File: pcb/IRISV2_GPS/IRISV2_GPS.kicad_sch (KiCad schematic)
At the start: 22 parts, among them U1 NEO-M9N, U2 lna

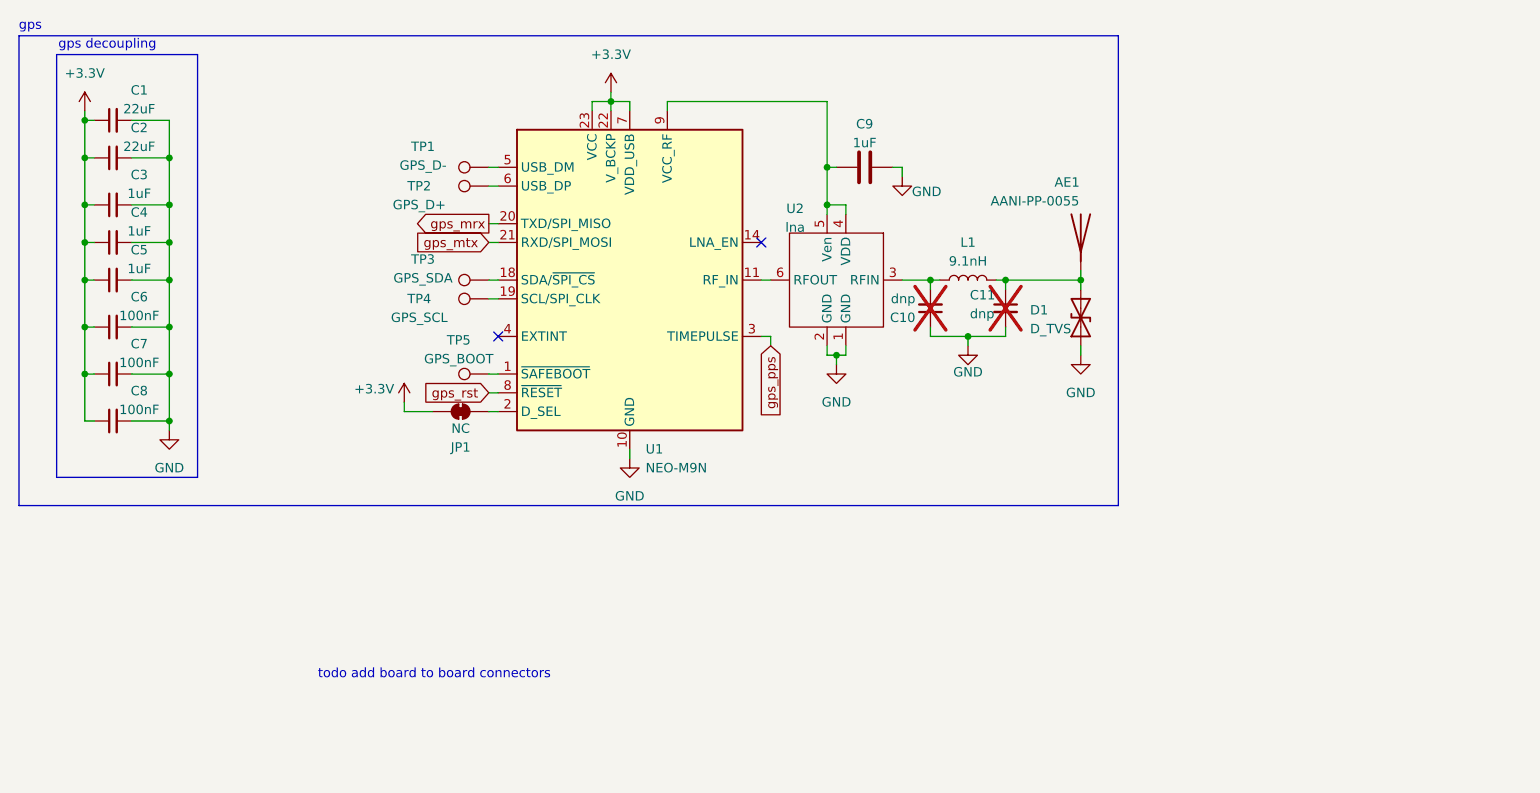
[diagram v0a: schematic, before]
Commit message: gps finished minus tvs (WHY ARE THEY ALL 0201), top layout + routing started
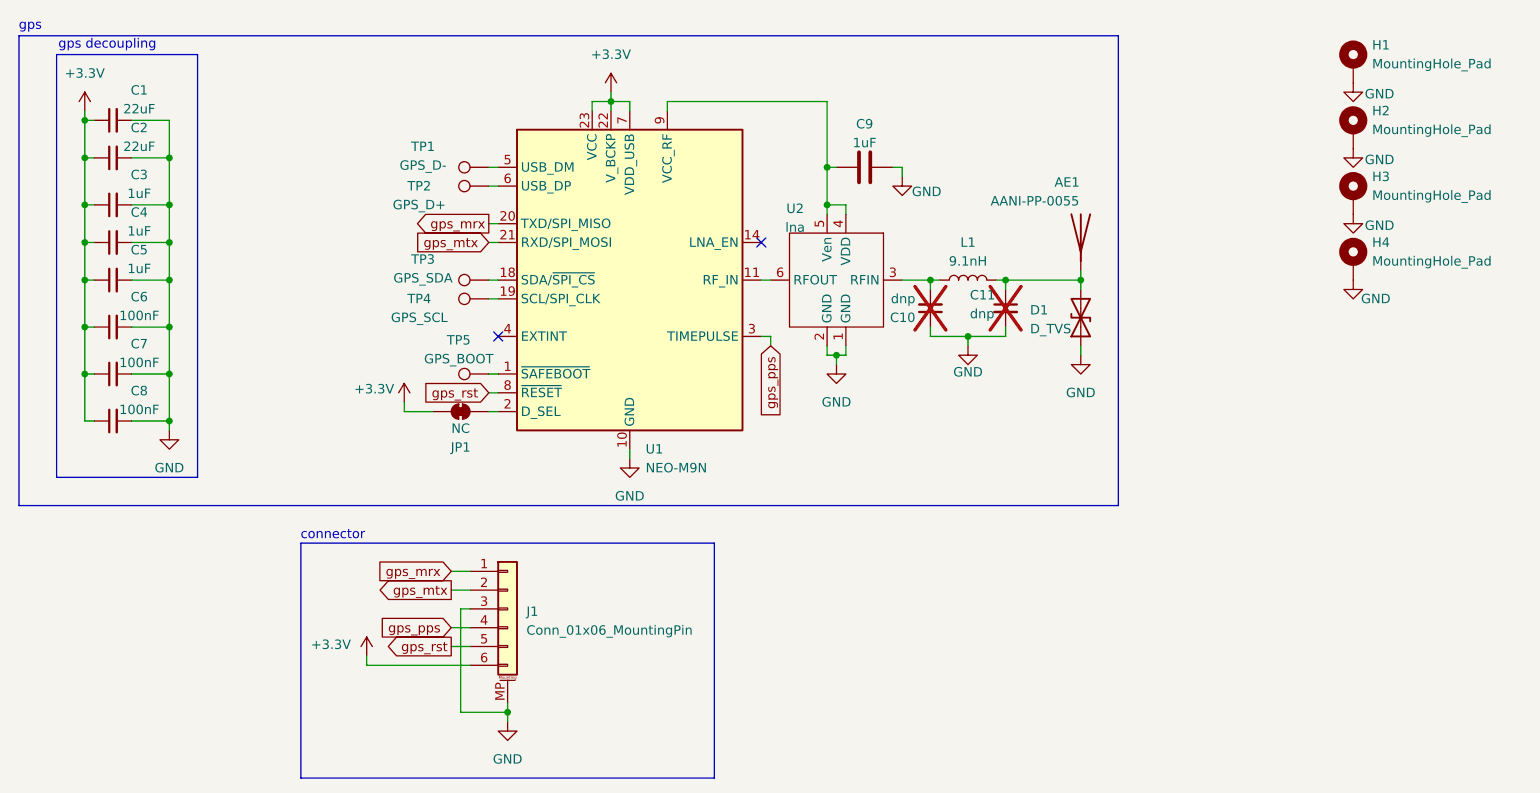
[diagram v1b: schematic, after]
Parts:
- added H1, H2, H3, H4: MountingHole_Pad, MountingHole:MountingHole_3.2mm_M3_ISO7380_Pad_TopBottom, symbol Mechanical:MountingHole_Pad
- added J1: Conn_01x06_MountingPin, Connector_JST:JST_PH_S6B-PH-SM4-TB_1x06-1MP_P2.00mm_Horizontal, symbol Connector_Generic_MountingPin:Conn_01x06_MountingPin
- JP1: footprint (none) -> Jumper:SolderJumper-2_P1.3mm_Bridged_RoundedPad1.0x1.5mm
- TP1, TP2, TP3, TP4, TP5: footprint (none) -> TestPoint:TestPoint_Pad_D2.0mm
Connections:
- net +3.3V: now also J1.6 (Pin_6)
- net GND: now also H1.1, H2.1, H3.1, H4.1, J1.3 (Pin_3), J1.MP (MountPin)
- net gps_mrx: now also J1.1 (Pin_1)
- net gps_mtx: now also J1.2 (Pin_2)
- net gps_pps: now also J1.4 (Pin_4)
- net gps_rst: now also J1.5 (Pin_5)
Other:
- note added: "connector"
- note removed: "todo add board to board connectors"

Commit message: removed high g accel, top board layout looking decent, routing started also - though i realized i was missing the micro sd card and that's going to be a pain to add
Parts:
- D1: footprint (none) -> Diode_SMD:D_0201_0603Metric
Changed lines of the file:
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@@
 			)
 		)
-		(property "Footprint" ""
+		(property "Footprint" "Diode_SMD:D_0201_0603Metric"
 			(at 191.77 99.06 0)
 			(effects
